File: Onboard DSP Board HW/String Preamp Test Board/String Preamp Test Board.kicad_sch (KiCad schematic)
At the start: 19 parts, among them J1 Battery, J4 Output Jack, U1 TLV9002, U2 TP4054

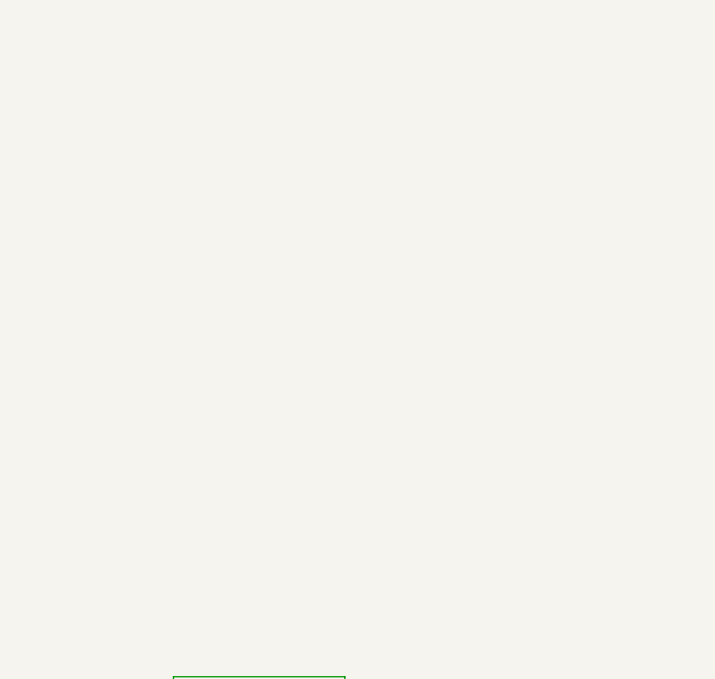
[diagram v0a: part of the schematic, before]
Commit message: Fix Opamp supplies, simulate, add safety resistor to V+
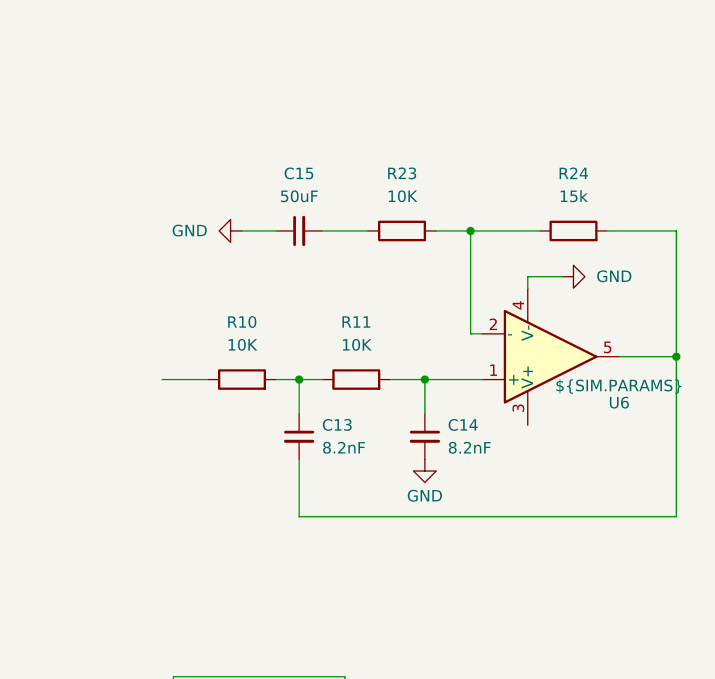
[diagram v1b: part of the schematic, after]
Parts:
- added C13, C14: 8.2nF, symbol Device:C_Small
- added C15: 50uF, symbol Device:C_Small
- added R10, R11, R23: 10K, symbol Device:R
- added R24: 15k, symbol Device:R
- added U6: ${SIM.PARAMS}, symbol Simulation_SPICE:OPAMP
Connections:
- net GND: now also C14.2, C15.1, U6.4 (V-)
- new net: C15.2, R23.1
- new net: C13.1, R10.2, R11.1
- new net: C13.2, R24.2, U6.5
- new net: C14.1, R11.2, U6.1 (+)
- new net: R23.2, R24.1, U6.2 (-)

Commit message: WIP
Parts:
- removed C5, C9: 4.7uF, Capacitor_SMD:C_0603_1608Metric, symbol Device:C
- removed C6, C8: 0.1uF, Capacitor_SMD:C_0603_1608Metric, symbol Device:C
- removed J1: Battery, Connector_JST:JST_PH_S2B-PH-K_1x02_P2.00mm_Horizontal, symbol Connector:Conn_01x02_Male
- removed J4: Output Jack, Connector_PinHeader_2.54mm:PinHeader_1x03_P2.54mm_Vertical, symbol Connector:Conn_01x03_Male
- removed R1, R2: 10k, Resistor_SMD:R_0603_1608Metric, symbol Device:R_US
- removed R7: 30k, Resistor_SMD:R_0603_1608Metric, symbol Device:R_US
- removed unit 2 of RV3
- removed unit 3 of U1
- removed U2: TP4054, Package_TO_SOT_SMD:SOT-23-5, symbol Battery_Management:MCP73811T-420I-OT
- added C16: 1uF, symbol Device:C_Small
- added C17, C18: 0.1uF, Capacitor_SMD:C_0603_1608Metric, symbol Device:C
- added R25, R26: 10k, Resistor_SMD:R_0603_1608Metric, symbol Device:R_US
- added U5: TLV9002, Package_TO_SOT_SMD:SOT-23-8, symbol Amplifier_Operational:Opamp_Dual
- added V1: VSIN, symbol Simulation_SPICE:VSIN
- added V2: 3.7, symbol Simulation_SPICE:VDC
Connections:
- net GND: now also C17.1, C18.1, R26.1, U5.4 (V-), V1.2, V2.2
- net v+: now also U6.3 (V+), C18.2, R25.2, U5.8 (V+), V2.1
- net vref: now also C17.2, R25.1, R26.2
- net sim_in: now reaches R20.1, RV1.2, U1.3 (+)
- net sim_in: now also V1.1
- net at C13.2, R24.2: now also RV2.2, U1.7; no longer U6.5
- net at U1.1, U1.2 (-): now also C16.1; no longer RV2.2
- net at C10.2, RV2.3: now also U6.1 (+); no longer U1.5 (+)
- net at C14.1, R11.2: now also U1.5 (+); no longer U6.1 (+)
- net at R23.2, R24.1: now also U1.6 (-); no longer U6.2 (-)
- net at R10.1: now also C16.2
- new net: C7.1, U6.2 (-), U6.5
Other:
- added sheet Lion Charger (charger.kicad_sch)
- moved on the sheet: C10, C13, C14, C15, C7, R10, R11, R20, R23, R24, R8, R9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
